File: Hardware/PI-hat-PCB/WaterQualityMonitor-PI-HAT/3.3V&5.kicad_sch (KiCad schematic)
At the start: 23 parts

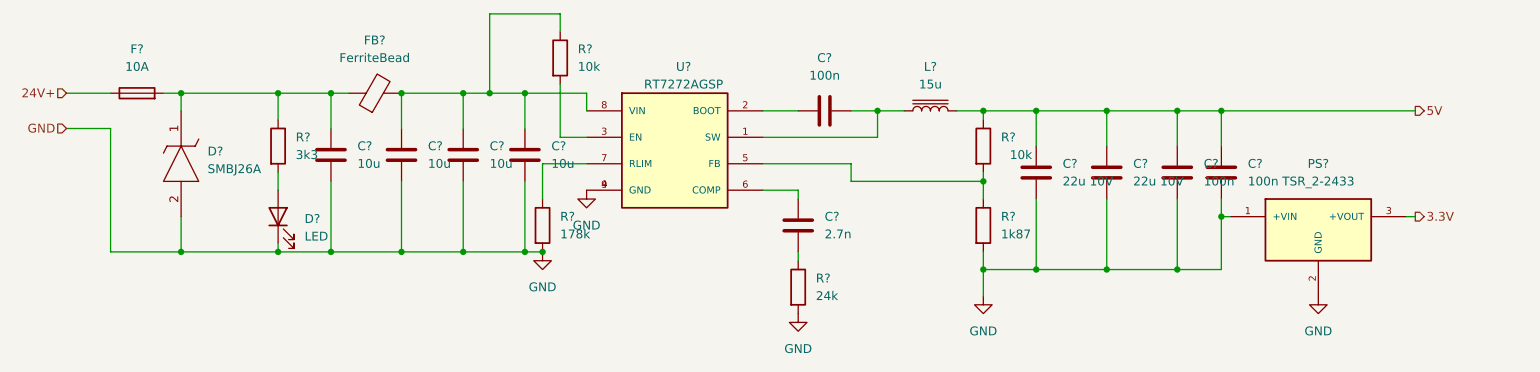
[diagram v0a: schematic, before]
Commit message: started heating and cooling design
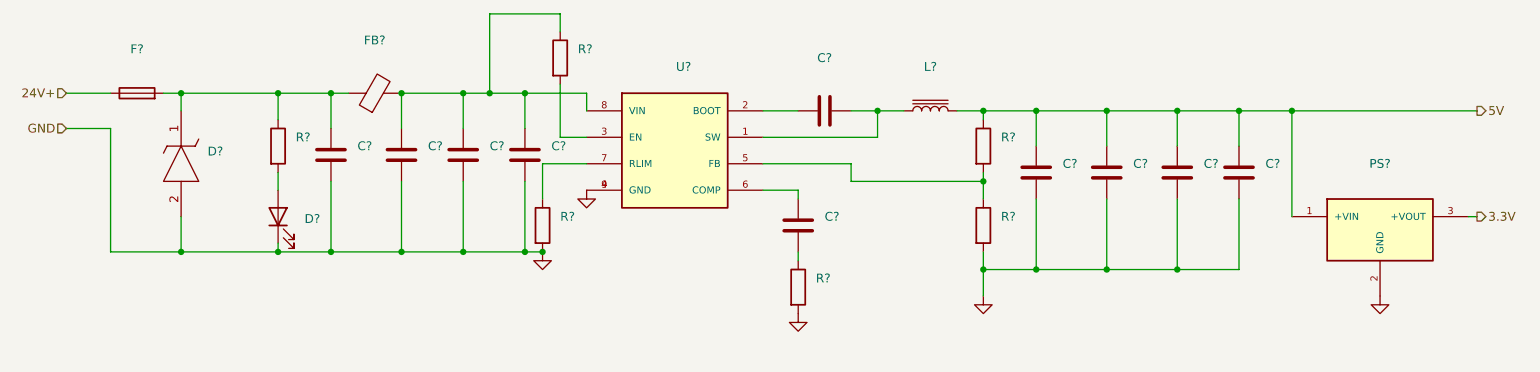
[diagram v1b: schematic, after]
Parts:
- C? (x4): value 10u -> (none)
- C? (x2): value 22u 10V -> (none)
- C? (x3): value 100n -> (none)
- C?: value 2.7n -> (none)
- D?: value LED -> (none)
- D?: value SMBJ26A -> (none); footprint DIOM5436X244N -> (none)
- F?: value 10A -> (none)
- FB?: value FerriteBead -> (none)
- L?: value 15u -> (none)
- PS?: value TSR_2-2433 -> (none); footprint CONV_TSR_2-2433 -> (none)
- R?: value 1k87 -> (none)
- R?: value 3k3 -> (none)
- R? (x2): value 10k -> (none)
- R?: value 24k -> (none)
- R?: value 178k -> (none)
- U?: value RT7272AGSP -> (none); footprint SOIC127P599X175-9N -> (none)
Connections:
- net 5V: now also PS?.1 (+VIN)
- net GND: no longer PS?.1 (+VIN)
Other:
- moved on the sheet: C?, PS?

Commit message: Enhanced schematics
Moved protection circuits to main schematic
changed tmc2208 VIO to 3.3V (5V is also fine)
added fuses to heat and cooling schematic
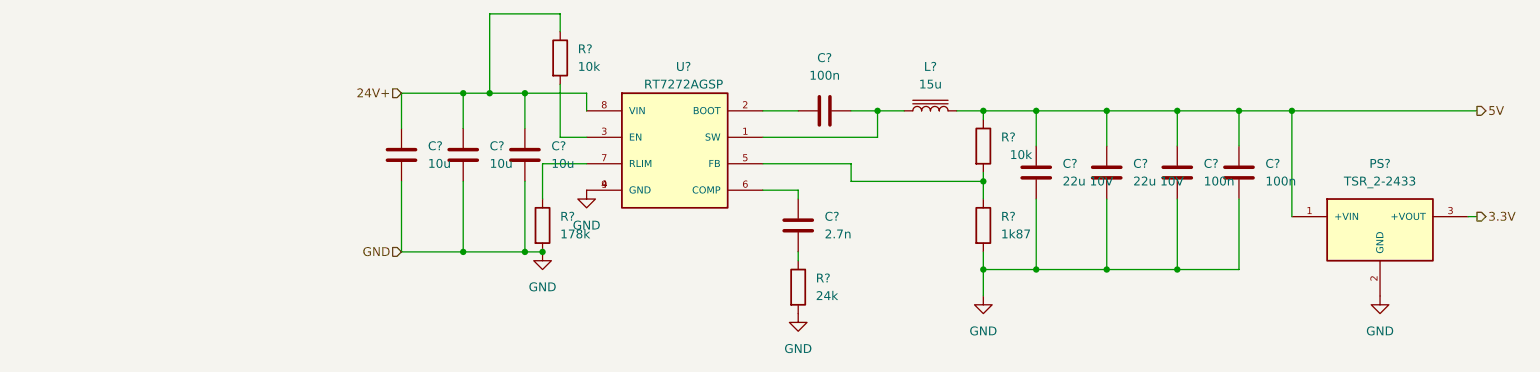
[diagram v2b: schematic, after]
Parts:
- removed C?: (no value), symbol Device:C
- removed D?: (no value), symbol Device:LED
- removed D?: (no value), symbol SamacSys_Parts:SMBJ26A
- removed F?: (no value), symbol Device:Fuse
- removed FB?: (no value), symbol Device:FerriteBead
- removed R?: (no value), symbol Device:R
- C? (x3): value (none) -> 10u
- C? (x2): value (none) -> 22u 10V
- C? (x3): value (none) -> 100n
- C?: value (none) -> 2.7n
- L?: value (none) -> 15u
- PS?: value (none) -> TSR_2-2433; footprint (none) -> CONV_TSR_2-2433
- R?: value (none) -> 1k87
- R? (x2): value (none) -> 10k
- R?: value (none) -> 24k
- R?: value (none) -> 178k
- U?: value (none) -> RT7272AGSP; footprint (none) -> SOIC127P599X175-9N
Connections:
- net 24V+: now also C?.1, C?.1, C?.1, R?.1, U?.8 (VIN)

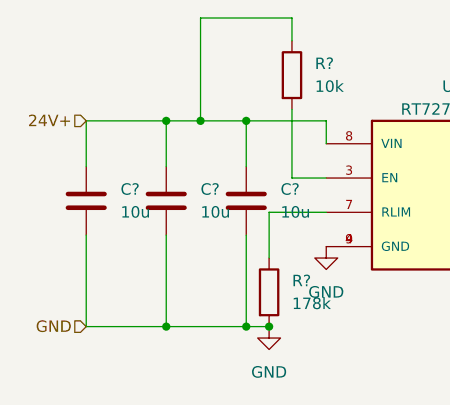
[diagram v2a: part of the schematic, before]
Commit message: changed PSU voltage from 24V to 12V
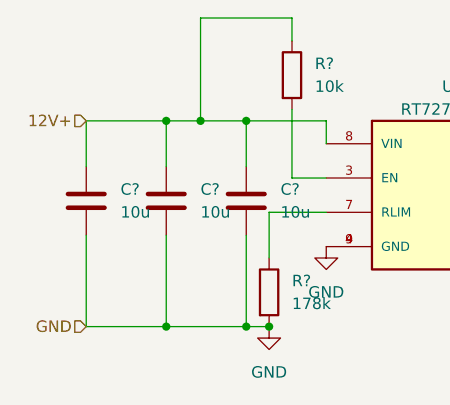
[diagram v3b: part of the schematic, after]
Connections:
- net 24V+ renamed 12V+
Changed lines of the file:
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@@
     (effects (font (size 1.27 1.27)) (justify left))
   )
-  (hierarchical_label "24V+" (shape input) (at 101.6 91.44 180)
+  (hierarchical_label "12V+" (shape input) (at 101.6 91.44 180)
     (effects (font (size 1.27 1.27)) (justify right))
   )

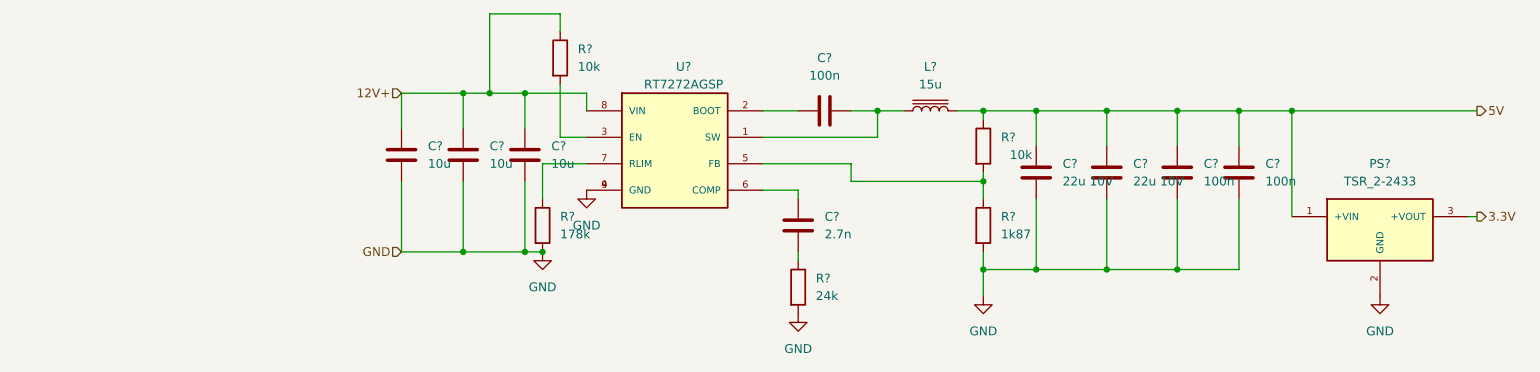
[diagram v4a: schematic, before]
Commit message: assigent footprints to all current components
I chose 1206smd handsolderable for caps and resistors and inductors, may need to be revised
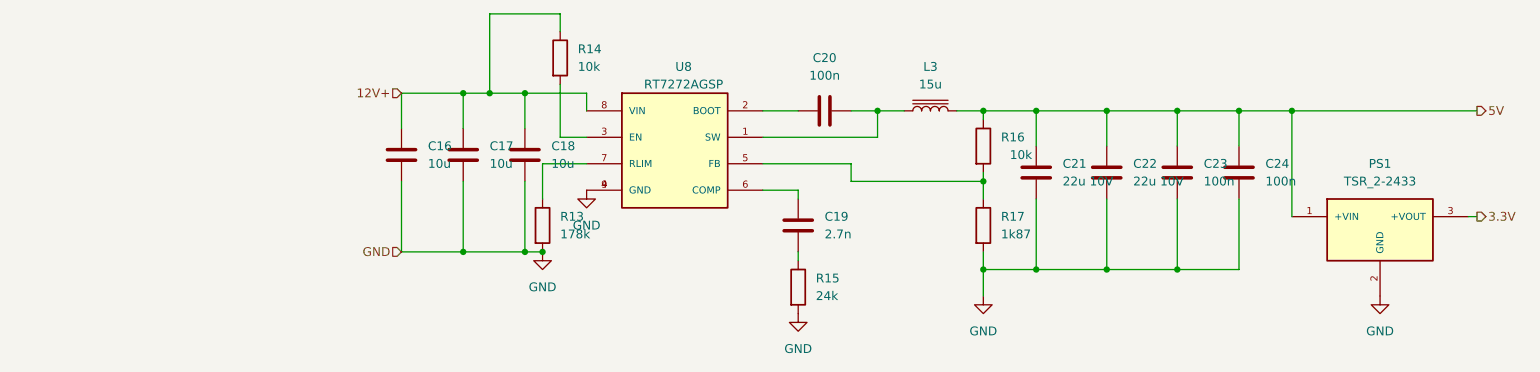
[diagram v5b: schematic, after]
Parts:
- C16, C17, C18, C19, C20, C21, C22, C23, C24: renamed from C?; footprint (none) -> Capacitor_SMD:C_1206_3216Metric_Pad1.33x1.80mm_HandSolder
- L3: renamed from L?; footprint (none) -> Inductor_SMD:L_1206_3216Metric_Pad1.22x1.90mm_HandSolder
- PS1: renamed from PS?; footprint CONV_TSR_2-2433 -> Converter_DCDC:Converter_DCDC_TRACO_TSR-1_THT
- R13, R14, R15, R16, R17: renamed from R?; footprint (none) -> Resistor_SMD:R_1206_3216Metric_Pad1.30x1.75mm_HandSolder
- U8: renamed from U?; footprint SOIC127P599X175-9N -> Snapeda:SOIC127P599X175-9N
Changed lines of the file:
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@@
   (symbol (lib_id "Device:R") (at 185.42 110.49 0) (unit 1)
     (in_bom yes) (on_board yes) (fields_autoplaced)
-    (property "Reference" "R?" (id 0) (at 187.96 109.2199 0)
+    (property "Reference" "R17" (id 0) (at 187.96 109.2199 0)
       (effects (font (size 1.27 1.27)) (justify left))
     )
@@
       (effects (font (size 1.27 1.27)) (justify left))
     )
-    (property "Footprint" "" (id 2) (at 183.642 110.49 90)
+    (property "Footprint" "Resistor_SMD:R_1206_3216Metric_Pad1.30x1.75mm_HandSolder" (id 2) (at 183.642 110.49 90)
       (effects (font (size 1.27 1.27)) hide)
     )
@@
   (symbol (lib_id "Device:C") (at 110.49 100.33 0) (unit 1)
     (in_bom yes) (on_board yes) (fields_autoplaced)
-    (property "Reference" "C?" (id 0) (at 114.3 99.0599 0)
+    (property "Reference" "C17" (id 0) (at 114.3 99.0599 0)
       (effects (font (size 1.27 1.27)) (justify left))
     )
@@
       (effects (font (size 1.27 1.27)) (justify left))
     )
-    (property "Footprint" "" (id 2) (at 111.4552 104.14 0)
+    (property "Footprint" "Capacitor_SMD:C_1206_3216Metric_Pad1.33x1.80mm_HandSolder" (id 2) (at 111.4552 104.14 0)
       (effects (font (size 1.27 1.27)) hide)
     )
@@
   (symbol (lib_id "Device:C") (at 203.2 102.87 180) (unit 1)
     (in_bom yes) (on_board yes) (fields_autoplaced)
-    (property "Reference" "C?" (id 0) (at 207.01 101.5999 0)
+    (property "Reference" "C22" (id 0) (at 207.01 101.5999 0)
       (effects (font (size 1.27 1.27)) (justify right))
     )
@@
       (effects (font (size 1.27 1.27)) (justify right))
     )
-    (property "Footprint" "" (id 2) (at 202.2348 99.06 0)
+    (property "Footprint" "Capacitor_SMD:C_1206_3216Metric_Pad1.33x1.80mm_HandSolder" (id 2) (at 202.2348 99.06 0)
       (effects (font (size 1.27 1.27)) hide)
     )
@@
   (symbol (lib_id "Device:C") (at 222.25 102.87 0) (mirror y) (unit 1)
     (in_bom yes) (on_board yes) (fields_autoplaced)
-    (property "Reference" "C?" (id 0) (at 226.06 101.5999 0)
+    (property "Reference" "C24" (id 0) (at 226.06 101.5999 0)
       (effects (font (size 1.27 1.27)) (justify right))
     )
@@
       (effects (font (size 1.27 1.27)) (justify right))
     )
-    (property "Footprint" "" (id 2) (at 221.2848 106.68 0)
+    (property "Footprint" "Capacitor_SMD:C_1206_3216Metric_Pad1.33x1.80mm_HandSolder" (id 2) (at 221.2848 106.68 0)
       (effects (font (size 1.27 1.27)) hide)
     )
@@
   (symbol (lib_id "Device:C") (at 193.04 102.87 180) (unit 1)
     (in_bom yes) (on_board yes) (fields_autoplaced)
-    (property "Reference" "C?" (id 0) (at 196.85 101.5999 0)
+    (property "Reference" "C21" (id 0) (at 196.85 101.5999 0)
       (effects (font (size 1.27 1.27)) (justify right))
     )
@@
       (effects (font (size 1.27 1.27)) (justify right))
     )
-    (property "Footprint" "" (id 2) (at 192.0748 99.06 0)
+    (property "Footprint" "Capacitor_SMD:C_1206_3216Metric_Pad1.33x1.80mm_HandSolder" (id 2) (at 192.0748 99.06 0)
       (effects (font (size 1.27 1.27)) hide)
     )
@@
   (symbol (lib_id "Device:R") (at 124.46 86.36 0) (unit 1)
     (in_bom yes) (on_board yes) (fields_autoplaced)
-    (property "Reference" "R?" (id 0) (at 127 85.0899 0)
+    (property "Reference" "R14" (id 0) (at 127 85.0899 0)
       (effects (font (size 1.27 1.27)) (justify left))
     )
@@
       (effects (font (size 1.27 1.27)) (justify left))
     )
-    (property "Footprint" "" (id 2) (at 122.682 86.36 90)
+    (property "Footprint" "Resistor_SMD:R_1206_3216Metric_Pad1.30x1.75mm_HandSolder" (id 2) (at 122.682 86.36 90)
       (effects (font (size 1.27 1.27)) hide)
     )
@@
   (symbol (lib_id "RT7272AGSP:RT7272AGSP") (at 142.24 101.6 0) (unit 1)
     (in_bom yes) (on_board yes) (fields_autoplaced)
-    (property "Reference" "U?" (id 0) (at 142.24 87.63 0))
+    (property "Reference" "U8" (id 0) (at 142.24 87.63 0))
     (property "Value" "RT7272AGSP" (id 1) (at 142.24 90.17 0))
-    (property "Footprint" "SOIC127P599X175-9N" (id 2) (at 133.35 110.49 0)
+    (property "Footprint" "Snapeda:SOIC127P599X175-9N" (id 2) (at 133.35 110.49 0)
       (effects (font (size 1.27 1.27)) (justify left bottom) hide)
     )
@@
   (symbol (lib_id "Device:R") (at 158.75 119.38 0) (unit 1)
     (in_bom yes) (on_board yes) (fields_autoplaced)
-    (property "Reference" "R?" (id 0) (at 161.29 118.1099 0)
+    (property "Reference" "R15" (id 0) (at 161.29 118.1099 0)
       (effects (font (size 1.27 1.27)) (justify left))
     )
@@
       (effects (font (size 1.27 1.27)) (justify left))
     )
-    (property "Footprint" "" (id 2) (at 156.972 119.38 90)
+    (property "Footprint" "Resistor_SMD:R_1206_3216Metric_Pad1.30x1.75mm_HandSolder" (id 2) (at 156.972 119.38 90)
       (effects (font (size 1.27 1.27)) hide)
     )
@@
   (symbol (lib_id "Device:C") (at 119.38 100.33 0) (unit 1)
     (in_bom yes) (on_board yes) (fields_autoplaced)
-    (property "Reference" "C?" (id 0) (at 123.19 99.0599 0)
+    (property "Reference" "C18" (id 0) (at 123.19 99.0599 0)
       (effects (font (size 1.27 1.27)) (justify left))
     )
@@
       (effects (font (size 1.27 1.27)) (justify left))
     )
-    (property "Footprint" "" (id 2) (at 120.3452 104.14 0)
+    (property "Footprint" "Capacitor_SMD:C_1206_3216Metric_Pad1.33x1.80mm_HandSolder" (id 2) (at 120.3452 104.14 0)
       (effects (font (size 1.27 1.27)) hide)
     )
@@
   (symbol (lib_id "Device:L_Iron") (at 177.8 93.98 90) (unit 1)
     (in_bom yes) (on_board yes) (fields_autoplaced)
-    (property "Reference" "L?" (id 0) (at 177.8 87.63 90))
+    (property "Reference" "L3" (id 0) (at 177.8 87.63 90))
     (property "Value" "15u" (id 1) (at 177.8 90.17 90))
-    (property "Footprint" "" (id 2) (at 177.8 93.98 0)
+    (property "Footprint" "Inductor_SMD:L_1206_3216Metric_Pad1.22x1.90mm_HandSolder" (id 2) (at 177.8 93.98 0)
       (effects (font (size 1.27 1.27)) hide)
     )
@@
   (symbol (lib_id "Device:R") (at 121.92 110.49 0) (unit 1)
     (in_bom yes) (on_board yes) (fields_autoplaced)
-    (property "Reference" "R?" (id 0) (at 124.46 109.2199 0)
+    (property "Reference" "R13" (id 0) (at 124.46 109.2199 0)
       (effects (font (size 1.27 1.27)) (justify left))
     )
@@
       (effects (font (size 1.27 1.27)) (justify left))
     )
-    (property "Footprint" "" (id 2) (at 120.142 110.49 90)
+    (property "Footprint" "Resistor_SMD:R_1206_3216Metric_Pad1.30x1.75mm_HandSolder" (id 2) (at 120.142 110.49 90)
       (effects (font (size 1.27 1.27)) hide)
     )
@@
   (symbol (lib_id "Device:C") (at 213.36 102.87 180) (unit 1)
     (in_bom yes) (on_board yes) (fields_autoplaced)
-    (property "Reference" "C?" (id 0) (at 217.17 101.5999 0)
+    (property "Reference" "C23" (id 0) (at 217.17 101.5999 0)
       (effects (font (size 1.27 1.27)) (justify right))
     )
@@
       (effects (font (size 1.27 1.27)) (justify right))
     )
-    (property "Footprint" "" (id 2) (at 212.3948 99.06 0)
+    (property "Footprint" "Capacitor_SMD:C_1206_3216Metric_Pad1.33x1.80mm_HandSolder" (id 2) (at 212.3948 99.06 0)
       (effects (font (size 1.27 1.27)) hide)
     )
@@
   (symbol (lib_id "Device:C") (at 101.6 100.33 0) (unit 1)
     (in_bom yes) (on_board yes) (fields_autoplaced)
-    (property "Reference" "C?" (id 0) (at 105.41 99.0599 0)
+    (property "Reference" "C16" (id 0) (at 105.41 99.0599 0)
       (effects (font (size 1.27 1.27)) (justify left))
     )
@@
       (effects (font (size 1.27 1.27)) (justify left))
     )
-    (property "Footprint" "" (id 2) (at 102.5652 104.14 0)
+    (property "Footprint" "Capacitor_SMD:C_1206_3216Metric_Pad1.33x1.80mm_HandSolder" (id 2) (at 102.5652 104.14 0)
       (effects (font (size 1.27 1.27)) hide)
     )
@@
   (symbol (lib_id "TSR_2-2433:TSR_2-2433") (at 242.57 111.76 0) (unit 1)
     (in_bom yes) (on_board yes) (fields_autoplaced)
-    (property "Reference" "PS?" (id 0) (at 242.57 101.6 0))
+    (property "Reference" "PS1" (id 0) (at 242.57 101.6 0))
     (property "Value" "TSR_2-2433" (id 1) (at 242.57 104.14 0))
-    (property "Footprint" "CONV_TSR_2-2433" (id 2) (at 250.19 116.84 0)
+    (property "Footprint" "Converter_DCDC:Converter_DCDC_TRACO_TSR-1_THT" (id 2) (at 250.19 116.84 0)
       (effects (font (size 1.27 1.27)) (justify left bottom) hide)
     )
@@
   (symbol (lib_id "Device:R") (at 185.42 99.06 0) (unit 1)
     (in_bom yes) (on_board yes)
-    (property "Reference" "R?" (id 0) (at 187.96 97.7899 0)
+    (property "Reference" "R16" (id 0) (at 187.96 97.7899 0)
       (effects (font (size 1.27 1.27)) (justify left))
     )
@@
       (effects (font (size 1.27 1.27)) (justify left))
     )
-    (property "Footprint" "" (id 2) (at 183.642 99.06 90)
+    (property "Footprint" "Resistor_SMD:R_1206_3216Metric_Pad1.30x1.75mm_HandSolder" (id 2) (at 183.642 99.06 90)
       (effects (font (size 1.27 1.27)) hide)
     )
@@
   (symbol (lib_id "Device:C") (at 158.75 110.49 180) (unit 1)
     (in_bom yes) (on_board yes) (fields_autoplaced)
-    (property "Reference" "C?" (id 0) (at 162.56 109.2199 0)
+    (property "Reference" "C19" (id 0) (at 162.56 109.2199 0)
       (effects (font (size 1.27 1.27)) (justify right))
     )
@@
       (effects (font (size 1.27 1.27)) (justify right))
     )
-    (property "Footprint" "" (id 2) (at 157.7848 106.68 0)
+    (property "Footprint" "Capacitor_SMD:C_1206_3216Metric_Pad1.33x1.80mm_HandSolder" (id 2) (at 157.7848 106.68 0)
       (effects (font (size 1.27 1.27)) hide)
     )
@@
   (symbol (lib_id "Device:C") (at 162.56 93.98 90) (unit 1)
     (in_bom yes) (on_board yes) (fields_autoplaced)
-    (property "Reference" "C?" (id 0) (at 162.56 86.36 90))
+    (property "Reference" "C20" (id 0) (at 162.56 86.36 90))
     (property "Value" "100n" (id 1) (at 162.56 88.9 90))
-    (property "Footprint" "" (id 2) (at 166.37 93.0148 0)
-      (effects (font (size 1.27 1.27)) hide)
-    )
+    (property "Footprint" "Capacitor_SMD:C_1206_3216Metric_Pad1.33x1.80mm_HandSolder" (id 2) (at 166.37 93.0148 0)
+      (effects (font (size 1.27 1.27)) hide)
+    )
